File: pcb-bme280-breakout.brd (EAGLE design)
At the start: 12.4 x 16.9 mm, 3 parts, among them U1 BME280

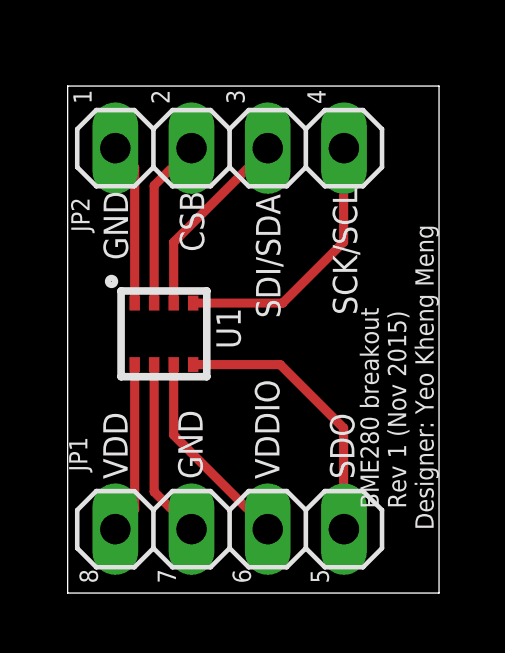
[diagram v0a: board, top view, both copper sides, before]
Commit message: mitre corners
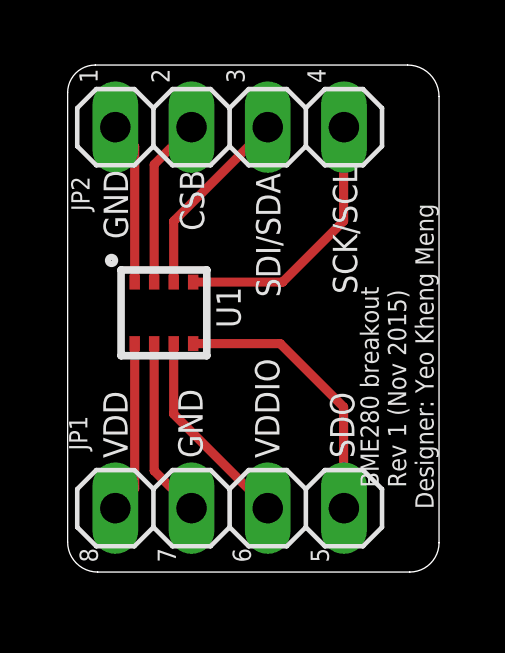
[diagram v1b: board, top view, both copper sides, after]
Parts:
- moved U1 0.70 mm to (3.21, 8.64)
- moved JP1 0.70 mm to (5.40, 2.13)
- moved JP2 0.70 mm to (5.40, 14.8)
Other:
- outline, holes or cut-outs redrawn
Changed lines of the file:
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@@
 <setting verticaltext="up"/>
 </settings>
-<grid distance="1" unitdist="mm" unit="mm" style="lines" multiple="1" display="no" altdistance="0.1" altunitdist="mm" altunit="mm"/>
+<grid distance="1" unitdist="mm" unit="mm" style="lines" multiple="1" display="yes" altdistance="0.1" altunitdist="mm" altunit="mm"/>
 <layers>
 <layer number="1" name="Top" color="4" fill="1" visible="yes" active="yes"/>
@@
 <board>
 <plain>
-<wire x1="0" y1="-0.7" x2="12.38" y2="-0.7" width="0" layer="20"/>
-<wire x1="12.38" y1="-0.7" x2="12.38" y2="16.2" width="0" layer="20"/>
-<wire x1="12.38" y1="16.2" x2="0" y2="16.2" width="0" layer="20"/>
-<wire x1="0" y1="16.2" x2="0" y2="-0.7" width="0" layer="20"/>
-<text x="2" y="3.1" size="0.8128" layer="21" rot="R90">VDD</text>
-<text x="4.5" y="3.1" size="0.8128" layer="21" rot="R90">GND</text>
-<text x="1.2" y="12.7" size="0.8128" layer="21" rot="R270">GND</text>
-<text x="3.74" y="12.7" size="0.8128" layer="21" rot="R270">CSB</text>
-<text x="7.06" y="3.1" size="0.8128" layer="21" rot="R90">VDDIO</text>
-<text x="6.28" y="12.6" size="0.8128" layer="21" rot="R270">SDI/SDA</text>
-<text x="9.56" y="3.1" size="0.8128" layer="21" rot="R90">SDO</text>
-<text x="8.84" y="12.8" size="0.8128" layer="21" rot="R270">SCK/SCL</text>
-<text x="12.2" y="1.4" size="0.6096" layer="21" rot="R90">   BME280 breakout
+<wire x1="12.38" y1="0.975909375" x2="12.38" y2="15.85195625" width="0" layer="20"/>
+<wire x1="12.38" y1="15.85195625" x2="11.33195625" y2="16.9" width="0" layer="20" curve="90"/>
+<wire x1="11.33195625" y1="16.9" x2="0.921953125" y2="16.9" width="0" layer="20"/>
+<wire x1="0.921953125" y1="16.9" x2="0" y2="15.978046875" width="0" layer="20" curve="90"/>
+<wire x1="0" y1="15.978046875" x2="0" y2="1" width="0" layer="20"/>
+<wire x1="0" y1="1" x2="1" y2="0" width="0" layer="20" curve="90"/>
+<wire x1="1" y1="0" x2="11.404090625" y2="0" width="0" layer="20"/>
+<wire x1="11.404090625" y1="0" x2="12.38" y2="0.975909375" width="0" layer="20" curve="90"/>
+<text x="2" y="3.8" size="0.8128" layer="21" rot="R90">VDD</text>
+<text x="4.5" y="3.8" size="0.8128" layer="21" rot="R90">GND</text>
+<text x="1.2" y="13.4" size="0.8128" layer="21" rot="R270">GND</text>
+<text x="3.74" y="13.4" size="0.8128" layer="21" rot="R270">CSB</text>
+<text x="7.06" y="3.8" size="0.8128" layer="21" rot="R90">VDDIO</text>
+<text x="6.28" y="13.3" size="0.8128" layer="21" rot="R270">SDI/SDA</text>
+<text x="9.56" y="3.8" size="0.8128" layer="21" rot="R90">SDO</text>
+<text x="8.84" y="13.5" size="0.8128" layer="21" rot="R270">SCK/SCL</text>
+<text x="12.2" y="2.1" size="0.6096" layer="21" rot="R90">   BME280 breakout
    Rev 1 (Nov 2015)
 Designer: Yeo Kheng Meng</text>
-<text x="0.8" y="15.6" size="0.6096" layer="21" rot="R90">1</text>
-<text x="3.4" y="15.6" size="0.6096" layer="21" rot="R90">2</text>
-<text x="5.9" y="15.6" size="0.6096" layer="21" rot="R90">3</text>
-<text x="8.6" y="15.6" size="0.6096" layer="21" rot="R90">4</text>
-<text x="8.1" y="0.1" size="0.6096" layer="21" rot="R270">5</text>
-<text x="5.5" y="0.1" size="0.6096" layer="21" rot="R270">6</text>
-<text x="3" y="0.1" size="0.6096" layer="21" rot="R270">7</text>
-<text x="0.4" y="0.1" size="0.6096" layer="21" rot="R270">8</text>
+<text x="1" y="16.3" size="0.6096" layer="21" rot="R90">1</text>
+<text x="3.4" y="16.3" size="0.6096" layer="21" rot="R90">2</text>
+<text x="5.9" y="16.3" size="0.6096" layer="21" rot="R90">3</text>
+<text x="8.6" y="16.3" size="0.6096" layer="21" rot="R90">4</text>
+<text x="8.1" y="0.8" size="0.6096" layer="21" rot="R270">5</text>
+<text x="5.5" y="0.8" size="0.6096" layer="21" rot="R270">6</text>
+<text x="3" y="0.8" size="0.6096" layer="21" rot="R270">7</text>
+<text x="0.4" y="0.8" size="0.6096" layer="21" rot="R270">8</text>
 </plain>
 <attributes>
@@
 </autorouter>
 <elements>
-<element name="U1" library="BME280ComponentLibrary" package="BME280_LGA" value="BME280" x="3.21" y="7.94" smashed="yes" rot="R90">
-<attribute name="PROD_ID" value="IC-13090" x="-4.41" y="1.59" size="1.778" layer="27" rot="R90" display="off"/>
-<attribute name="NAME" x="5.77" y="7.435" size="0.8128" layer="25" font="vector" rot="R90"/>
+<element name="U1" library="BME280ComponentLibrary" package="BME280_LGA" value="BME280" x="3.21" y="8.64" smashed="yes" rot="R90">
+<attribute name="PROD_ID" value="IC-13090" x="-4.41" y="2.29" size="1.778" layer="27" rot="R90" display="off"/>
+<attribute name="NAME" x="5.77" y="8.135" size="0.8128" layer="25" font="vector" rot="R90"/>
 </element>
-<element name="JP1" library="pinhead+" package="1X04" value="" x="5.4" y="1.43" smashed="yes" rot="R180">
-<attribute name="NAME" x="0.0488" y="4.5062" size="0.6096" layer="25" ratio="10" rot="R270"/>
-<attribute name="VALUE" x="10.48" y="4.605" size="1.27" layer="27" rot="R180"/>
+<element name="JP1" library="pinhead+" package="1X04" value="" x="5.4" y="2.13" smashed="yes" rot="R180">
+<attribute name="NAME" x="0.0488" y="5.2062" size="0.6096" layer="25" ratio="10" rot="R270"/>
+<attribute name="VALUE" x="10.48" y="5.305" size="1.27" layer="27" rot="R180"/>
 </element>
-<element name="JP2" library="pinhead+" package="1X04" value="" x="5.4" y="14.13" smashed="yes">
-<attribute name="NAME" x="0.7312" y="11.3338" size="0.6096" layer="25" ratio="10" rot="R90"/>
-<attribute name="VALUE" x="0.32" y="10.955" size="1.27" layer="27"/>
+<element name="JP2" library="pinhead+" package="1X04" value="" x="5.4" y="14.83" smashed="yes">
+<attribute name="NAME" x="0.7312" y="12.0338" size="0.6096" layer="25" ratio="10" rot="R90"/>
+<attribute name="VALUE" x="0.32" y="11.655" size="1.27" layer="27"/>
 </element>
 </elements>
@@
 <contactref element="U1" pad="P$8"/>
 <contactref element="JP1" pad="4"/>
-<wire x1="2.235" y1="6.915" x2="2.235" y2="2.075" width="0.3048" layer="1"/>
-<wire x1="2.235" y1="2.075" x2="1.59" y2="1.43" width="0.3048" layer="1"/>
+<wire x1="2.235" y1="7.615" x2="2.235" y2="2.775" width="0.3048" layer="1"/>
+<wire x1="2.235" y1="2.775" x2="1.59" y2="2.13" width="0.3048" layer="1"/>
 </signal>
 <signal name="N$2">
 <contactref element="U1" pad="P$7"/>
 <contactref element="JP1" pad="3"/>
-<wire x1="2.885" y1="6.915" x2="2.885" y2="2.675" width="0.3048" layer="1"/>
-<wire x1="2.885" y1="2.675" x2="4.13" y2="1.43" width="0.3048" layer="1"/>
+<wire x1="2.885" y1="7.615" x2="2.885" y2="3.375" width="0.3048" layer="1"/>
+<wire x1="2.885" y1="3.375" x2="4.13" y2="2.13" width="0.3048" layer="1"/>
 </signal>
 <signal name="N$3">
 <contactref element="U1" pad="P$6"/>
 <contactref element="JP1" pad="2"/>
-<wire x1="3.535" y1="6.915" x2="3.535" y2="4.565" width="0.3048" layer="1"/>
-<wire x1="3.535" y1="4.565" x2="6.67" y2="1.43" width="0.3048" layer="1"/>
+<wire x1="3.535" y1="7.615" x2="3.535" y2="5.265" width="0.3048" layer="1"/>
+<wire x1="3.535" y1="5.265" x2="6.67" y2="2.13" width="0.3048" layer="1"/>
 </signal>
 <signal name="N$4">
 <contactref element="U1" pad="P$5"/>
 <contactref element="JP1" pad="1"/>
-<wire x1="4.185" y1="6.915" x2="7.085" y2="6.915" width="0.3048" layer="1"/>
-<wire x1="7.085" y1="6.915" x2="9.2" y2="4.8" width="0.3048" layer="1"/>
-<wire x1="9.2" y1="4.8" x2="9.2" y2="1.44" width="0.3048" layer="1"/>
-<wire x1="9.2" y1="1.44" x2="9.21" y2="1.43" width="0.3048" layer="1"/>
+<wire x1="4.185" y1="7.615" x2="7.085" y2="7.615" width="0.3048" layer="1"/>
+<wire x1="7.085" y1="7.615" x2="9.2" y2="5.5" width="0.3048" layer="1"/>
+<wire x1="9.2" y1="5.5" x2="9.2" y2="2.14" width="0.3048" layer="1"/>
+<wire x1="9.2" y1="2.14" x2="9.21" y2="2.13" width="0.3048" layer="1"/>
 </signal>
 <signal name="N$5">
 <contactref element="U1" pad="P$4"/>
 <contactref element="JP2" pad="4"/>
-<wire x1="4.185" y1="8.965" x2="7.165" y2="8.965" width="0.3048" layer="1"/>
-<wire x1="7.165" y1="8.965" x2="9.2" y2="11" width="0.3048" layer="1"/>
-<wire x1="9.2" y1="11" x2="9.2" y2="14.12" width="0.3048" layer="1"/>
-<wire x1="9.2" y1="14.12" x2="9.21" y2="14.13" width="0.3048" layer="1"/>
+<wire x1="4.185" y1="9.665" x2="7.165" y2="9.665" width="0.3048" layer="1"/>
+<wire x1="7.165" y1="9.665" x2="9.2" y2="11.7" width="0.3048" layer="1"/>
+<wire x1="9.2" y1="11.7" x2="9.2" y2="14.82" width="0.3048" layer="1"/>
+<wire x1="9.2" y1="14.82" x2="9.21" y2="14.83" width="0.3048" layer="1"/>
 </signal>
 <signal name="N$6">
 <contactref element="U1" pad="P$3"/>
 <contactref element="JP2" pad="3"/>
-<wire x1="3.535" y1="8.965" x2="3.535" y2="10.995" width="0.3048" layer="1"/>
-<wire x1="3.535" y1="10.995" x2="6.67" y2="14.13" width="0.3048" layer="1"/>
+<wire x1="3.535" y1="9.665" x2="3.535" y2="11.695" width="0.3048" layer="1"/>
+<wire x1="3.535" y1="11.695" x2="6.67" y2="14.83" width="0.3048" layer="1"/>
 </signal>
 <signal name="N$7">
 <contactref element="U1" pad="P$2"/>
 <contactref element="JP2" pad="2"/>
-<wire x1="2.885" y1="8.965" x2="2.885" y2="12.885" width="0.3048" layer="1"/>
-<wire x1="2.885" y1="12.885" x2="4.13" y2="14.13" width="0.3048" layer="1"/>
+<wire x1="2.885" y1="9.665" x2="2.885" y2="13.585" width="0.3048" layer="1"/>
+<wire x1="2.885" y1="13.585" x2="4.13" y2="14.83" width="0.3048" layer="1"/>
 </signal>
 <signal name="N$8">
 <contactref element="U1" pad="P$1"/>
 <contactref element="JP2" pad="1"/>
-<wire x1="2.235" y1="8.965" x2="2.235" y2="13.485" width="0.3048" layer="1"/>
-<wire x1="2.235" y1="13.485" x2="1.59" y2="14.13" width="0.3048" layer="1"/>
+<wire x1="2.235" y1="9.665" x2="2.235" y2="14.185" width="0.3048" layer="1"/>
+<wire x1="2.235" y1="14.185" x2="1.59" y2="14.83" width="0.3048" layer="1"/>
 </signal>
 </signals>
